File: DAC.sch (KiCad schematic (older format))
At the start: 16 parts, among them Q1 MJD31CT4G, U3 MCP4728, U4 TLV2371

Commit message: Added current-limiting resistors on the LCD backlight
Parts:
- removed C7: 4u7/25V, Capacitors_SMD:C_0805, symbol C
- added R10, R11, R12, R13, R8, R9: 6R8, Resistors_SMD:R_0805, symbol R
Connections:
- net +12V: now also R13.1; no longer Q1.2 (C)
- new net: Q1.2 (C), R8.2
- new net: R8.1, R9.2
- new net: R10.2, R9.1
- new net: R10.1, R11.2
- new net: R11.1, R12.2
- new net: R12.1, R13.2
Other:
- moved on the sheet: C3, C4, C5, C6, PP3, PP4, Q1, R2, R3, R4, R5, R6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

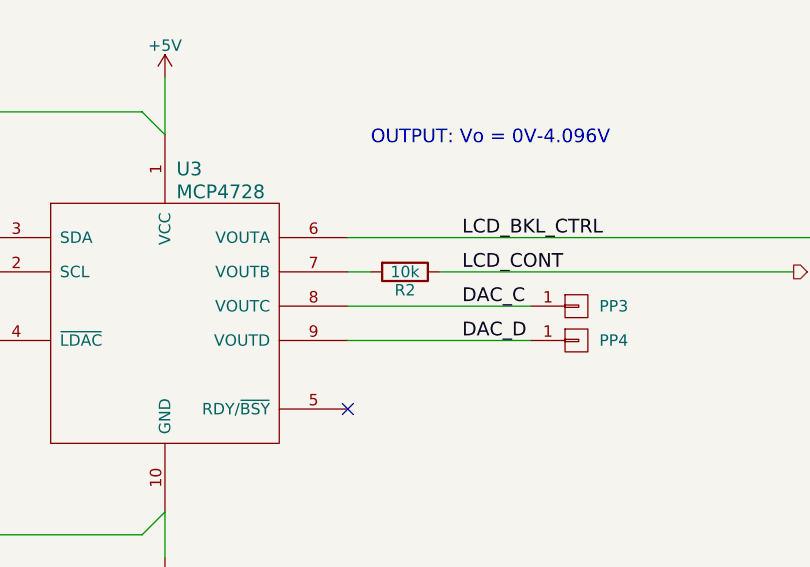
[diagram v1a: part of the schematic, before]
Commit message: Changed resistors on the PCB
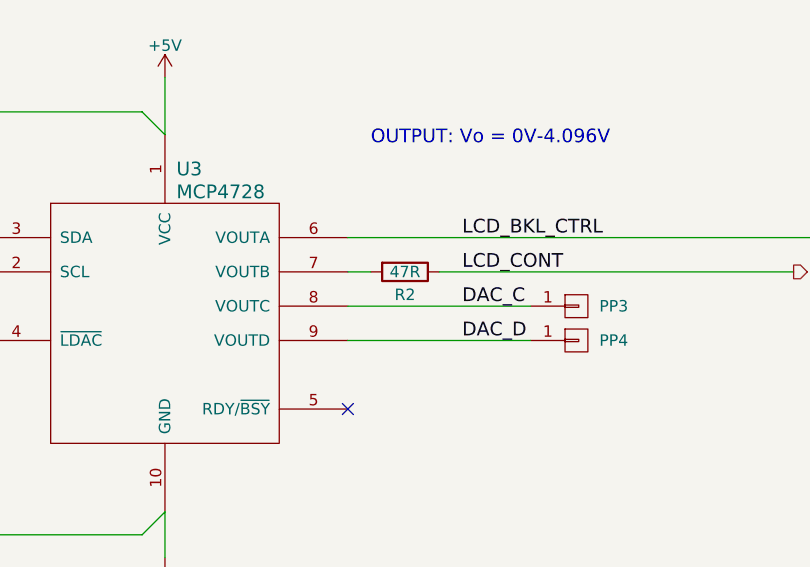
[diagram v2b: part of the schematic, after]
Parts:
- R10, R11, R12, R13, R8, R9: Order Code 2447032 -> 9333517; Part Number MCWR08W6R80FTL -> MC01W080516R8
- R2: value 10k -> 47R; Alt. Order Code 71-CRCW0805-10K-E3 -> 667-ERJ-6GEYJ470V; Note 10kΩ/1% 0805 resistor -> 47Ω/1% 0805 resistor; Order Code 2073607 -> 2447666; Part Number MCMR08X1002FTL -> MCWR08X47R0FTL
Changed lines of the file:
@@
 Text Label 4200 2350 0    60   ~ 0
 LCD_CONT
-$Comp
-L R R2
-U 1 1 56EC08D7
-P 3950 2350
-F 0 "R2" V 4030 2350 50  0000 C CNN
-F 1 "10k" V 3950 2350 50  0000 C CNN
-F 2 "Resistors_SMD:R_0805" V 3880 2350 50  0001 C CNN
-F 3 "" H 3950 2350 50  0000 C CNN
-F 4 "MCMR08X1002FTL" V 3950 2350 60  0001 C CNN "Part Number"
-F 5 "Multicomp" V 3950 2350 60  0001 C CNN "Manufacturer"
-F 6 "0805" H 3950 2350 60  0001 C CNN "Package"
-F 7 "Farnell" H 3950 2350 60  0001 C CNN "Supplier"
-F 8 "2073607" V 3950 2350 60  0001 C CNN "Order Code"
-F 9 "Mouser" H 3950 2350 60  0001 C CNN "Alt. Supplier"
-F 10 "71-CRCW0805-10K-E3" H 3950 2350 60  0001 C CNN "Alt. Order Code"
-F 11 "10kΩ/1% 0805 resistor" H 3950 2350 60  0001 C CNN "Note"
-	1    3950 2350
-	0    1    1    0
-$EndComp
 Wire Wire Line
 	3700 2350 3800 2350
@@
 F 2 "Resistors_SMD:R_0805" V 9730 1950 50  0001 C CNN
 F 3 "" H 9800 1950 50  0000 C CNN
-F 4 "MCWR08W6R80FTL" H 9800 1950 60  0001 C CNN "Part Number"
+F 4 "MC01W080516R8" H 9800 1950 60  0001 C CNN "Part Number"
 F 5 "Multicomp" H 9800 1950 60  0001 C CNN "Manufacturer"
 F 6 "0805" H 9800 1950 60  0001 C CNN "Package"
 F 7 "Farnell" H 9800 1950 60  0001 C CNN "Supplier"
-F 8 "2447032" H 9800 1950 60  0001 C CNN "Order Code"
+F 8 "9333517" H 9800 1950 60  0001 C CNN "Order Code"
 F 9 "Mouser" H 9800 1950 60  0001 C CNN "Alt. Supplier"
 F 10 "603-RC0805FR-076R8L" H 9800 1950 60  0001 C CNN "Alt. Order Code"
@@
 F 2 "Resistors_SMD:R_0805" V 9830 1550 50  0001 C CNN
 F 3 "" H 9900 1550 50  0000 C CNN
-F 4 "MCWR08W6R80FTL" H 9900 1550 60  0001 C CNN "Part Number"
+F 4 "MC01W080516R8" H 9900 1550 60  0001 C CNN "Part Number"
 F 5 "Multicomp" H 9900 1550 60  0001 C CNN "Manufacturer"
 F 6 "0805" H 9900 1550 60  0001 C CNN "Package"
 F 7 "Farnell" H 9900 1550 60  0001 C CNN "Supplier"
-F 8 "2447032" H 9900 1550 60  0001 C CNN "Order Code"
+F 8 "9333517" H 9900 1550 60  0001 C CNN "Order Code"
 F 9 "Mouser" H 9900 1550 60  0001 C CNN "Alt. Supplier"
 F 10 "603-RC0805FR-076R8L" H 9900 1550 60  0001 C CNN "Alt. Order Code"
@@
 F 2 "Resistors_SMD:R_0805" V 9930 1150 50  0001 C CNN
 F 3 "" H 10000 1150 50  0000 C CNN
-F 4 "MCWR08W6R80FTL" H 10000 1150 60  0001 C CNN "Part Number"
+F 4 "MC01W080516R8" H 10000 1150 60  0001 C CNN "Part Number"
 F 5 "Multicomp" H 10000 1150 60  0001 C CNN "Manufacturer"
 F 6 "0805" H 10000 1150 60  0001 C CNN "Package"
 F 7 "Farnell" H 10000 1150 60  0001 C CNN "Supplier"
-F 8 "2447032" H 10000 1150 60  0001 C CNN "Order Code"
+F 8 "9333517" H 10000 1150 60  0001 C CNN "Order Code"
 F 9 "Mouser" H 10000 1150 60  0001 C CNN "Alt. Supplier"
 F 10 "603-RC0805FR-076R8L" H 10000 1150 60  0001 C CNN "Alt. Order Code"
@@
 F 2 "Resistors_SMD:R_0805" V 10430 1950 50  0001 C CNN
 F 3 "" H 10500 1950 50  0000 C CNN
-F 4 "MCWR08W6R80FTL" H 10500 1950 60  0001 C CNN "Part Number"
+F 4 "MC01W080516R8" H 10500 1950 60  0001 C CNN "Part Number"
 F 5 "Multicomp" H 10500 1950 60  0001 C CNN "Manufacturer"
 F 6 "0805" H 10500 1950 60  0001 C CNN "Package"
 F 7 "Farnell" H 10500 1950 60  0001 C CNN "Supplier"
-F 8 "2447032" H 10500 1950 60  0001 C CNN "Order Code"
+F 8 "9333517" H 10500 1950 60  0001 C CNN "Order Code"
 F 9 "Mouser" H 10500 1950 60  0001 C CNN "Alt. Supplier"
 F 10 "603-RC0805FR-076R8L" H 10500 1950 60  0001 C CNN "Alt. Order Code"
@@
 F 2 "Resistors_SMD:R_0805" V 10530 1550 50  0001 C CNN
 F 3 "" H 10600 1550 50  0000 C CNN
-F 4 "MCWR08W6R80FTL" H 10600 1550 60  0001 C CNN "Part Number"
+F 4 "MC01W080516R8" H 10600 1550 60  0001 C CNN "Part Number"
 F 5 "Multicomp" H 10600 1550 60  0001 C CNN "Manufacturer"
 F 6 "0805" H 10600 1550 60  0001 C CNN "Package"
 F 7 "Farnell" H 10600 1550 60  0001 C CNN "Supplier"
-F 8 "2447032" H 10600 1550 60  0001 C CNN "Order Code"
+F 8 "9333517" H 10600 1550 60  0001 C CNN "Order Code"
 F 9 "Mouser" H 10600 1550 60  0001 C CNN "Alt. Supplier"
 F 10 "603-RC0805FR-076R8L" H 10600 1550 60  0001 C CNN "Alt. Order Code"
@@
 F 2 "Resistors_SMD:R_0805" V 10630 1150 50  0001 C CNN
 F 3 "" H 10700 1150 50  0000 C CNN
-F 4 "MCWR08W6R80FTL" H 10700 1150 60  0001 C CNN "Part Number"
+F 4 "MC01W080516R8" H 10700 1150 60  0001 C CNN "Part Number"
 F 5 "Multicomp" H 10700 1150 60  0001 C CNN "Manufacturer"
 F 6 "0805" H 10700 1150 60  0001 C CNN "Package"
 F 7 "Farnell" H 10700 1150 60  0001 C CNN "Supplier"
-F 8 "2447032" H 10700 1150 60  0001 C CNN "Order Code"
+F 8 "9333517" H 10700 1150 60  0001 C CNN "Order Code"
 F 9 "Mouser" H 10700 1150 60  0001 C CNN "Alt. Supplier"
 F 10 "603-RC0805FR-076R8L" H 10700 1150 60  0001 C CNN "Alt. Order Code"
@@
 Wire Wire Line
 	10500 2150 10300 2150
+$Comp
+L R R2
+U 1 1 576D8336
+P 3950 2350
+F 0 "R2" V 4050 2350 50  0000 C CNN
+F 1 "47R" V 3950 2350 50  0000 C CNN
+F 2 "Resistors_SMD:R_0805" V 3880 2350 50  0001 C CNN
+F 3 "" H 3950 2350 50  0000 C CNN
+F 4 "MCWR08X47R0FTL" H 3950 2350 60  0001 C CNN "Part Number"
+F 5 "Multicomp" H 3950 2350 60  0001 C CNN "Manufacturer"
+F 6 "0805" H 3950 2350 60  0001 C CNN "Package"
+F 7 "Farnell" H 3950 2350 60  0001 C CNN "Supplier"
+F 8 "2447666" H 3950 2350 60  0001 C CNN "Order Code"
+F 9 "Mouser" H 3950 2350 60  0001 C CNN "Alt. Supplier"
+F 10 "667-ERJ-6GEYJ470V" H 3950 2350 60  0001 C CNN "Alt. Order Code"
+F 11 "47Ω/1% 0805 resistor" H 3950 2350 60  0001 C CNN "Note"
+	1    3950 2350
+	0    1    1    0
+$EndComp
 $EndSCHEMATC
